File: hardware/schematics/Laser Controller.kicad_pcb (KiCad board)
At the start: 2 copper layers, 118 x 90 mm, 57 parts, among them J1 Micro_SD_Card, J2 PWR IN +5V, J3 PWR IN Galvo, U1 ESP32-S3-N16R8-DevKit, U10 DS18B20, U12 OPA4134UA_2K5, U13 Galvo Input, U15 6N137, U16 6N137, U17 6N137, U2 DAC8562SDGST, U3 TTL_RGB Blue, U4 TTL_RGB Red, U5 TTL_RGB Green, U6 DS18B20, U7 DS18B20, U8 DS18B20, U9 DS18B20

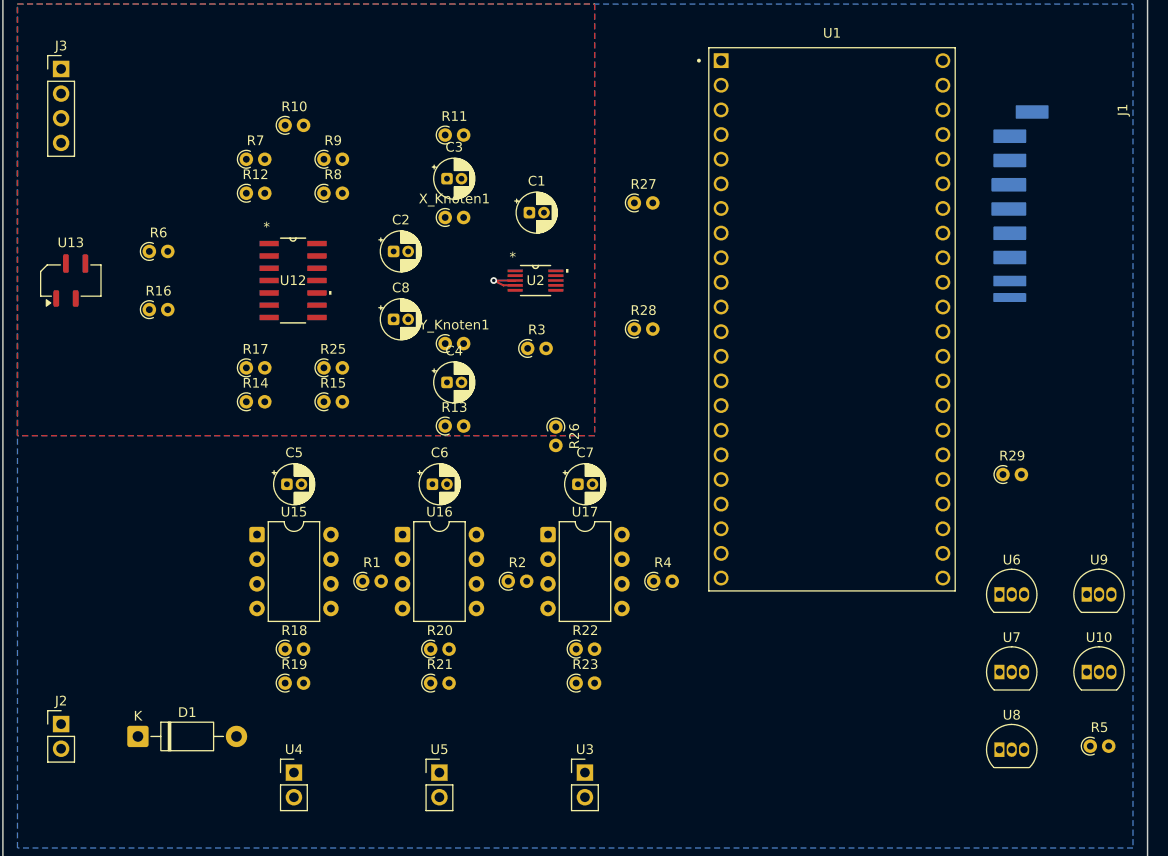
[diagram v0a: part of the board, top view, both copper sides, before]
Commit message: hw: copper happened - Freerouting did 92 nets in 19 seconds, 31 of them badly
Wired up the KiCAD MCP server and let Freerouting 2.0.1 loose on the board.
274 tracks, 10 vias, zero unconnected items. Not fab-ready: 31 clearance
violations survive, 20 of them under 0.10 mm, and they are not spread evenly -
they sit on the two fine-pitch parts where the router tried to thread traces
between pads that have no room between them.

- Added Laser Controller.kicad_pro with a Power net class and 0.2 mm design
  rules, so the board finally has somewhere to keep its rules
- Power traces widened after SES import: +-15V / 5V rails 0.6 mm, +3V3 and
  grounds 0.5 mm, signals stay at 0.2 mm
- Zones refilled after import - without that, DRC screams 283 zero-clearance
  errors that are pure artifact
- LAYOUT.md documents the remaining violations by location, plus two
  Freerouting quirks: it exports everything at a fixed 200 um in one
  kicad_default class (the Power net class never reaches it), and the SES
  import leaves pours unfilled
- .gitignore now swallows .dsn/.ses/.kicad_prl/DRC json

Next: rip up and hand-route the U2 and U12 fanouts. Worth doing by hand
regardless - an autorouter has no opinion about feedback loop length or which
side of a split ground plane a return current belongs on.
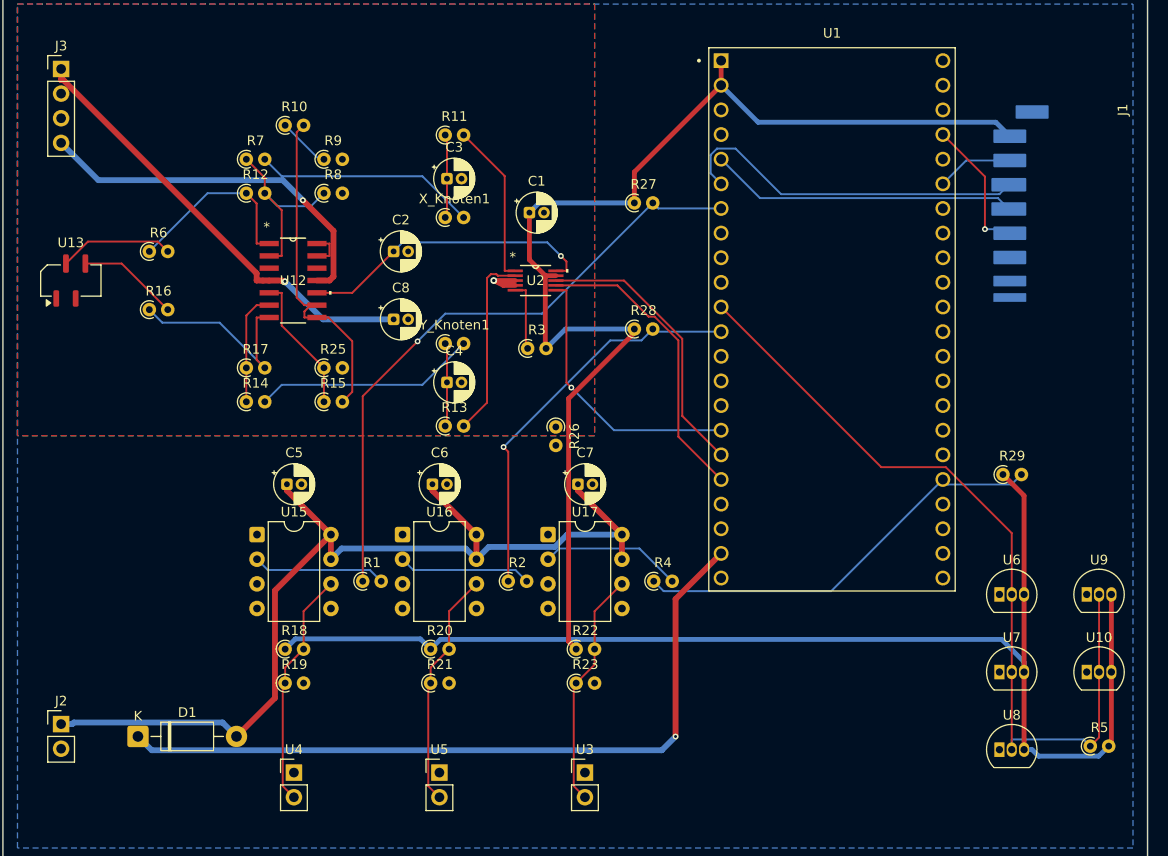
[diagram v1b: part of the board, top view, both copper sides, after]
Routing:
- net +3V3: track 0.00 -> 258.3 mm
- net Buck +5V: track 0.00 -> 104.4 mm
- net Net-(U1-GPIO18): track 0.00 -> 87.4 mm
- net /+5V_MCU: track 0.00 -> 77.4 mm, vias 0 -> 1
- net /GPIO7: track 0.00 -> 64.5 mm, vias 0 -> 1
- net +15V: track 0.00 -> 46.1 mm, vias 0 -> 1
- net /GPIO21: track 0.00 -> 43.7 mm
- net /GPIO8: track 0.00 -> 41.6 mm, vias 0 -> 1
- net -15V: track 0.00 -> 38.4 mm, vias 0 -> 1
- net Net-(J1-MOSI): track 0.00 -> 36.8 mm
- net /VREF_BUF: track 0.00 -> 34.6 mm
- net Net-(J1-CLK): track 0.00 -> 31.8 mm
- net Net-(U1-GPIO12): track 0.00 -> 31.1 mm
- net Net-(U12-+IN_C): track 0.00 -> 30.7 mm, vias 0 -> 1
- net Net-(U1-GPIO11): track 0.00 -> 29.1 mm
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
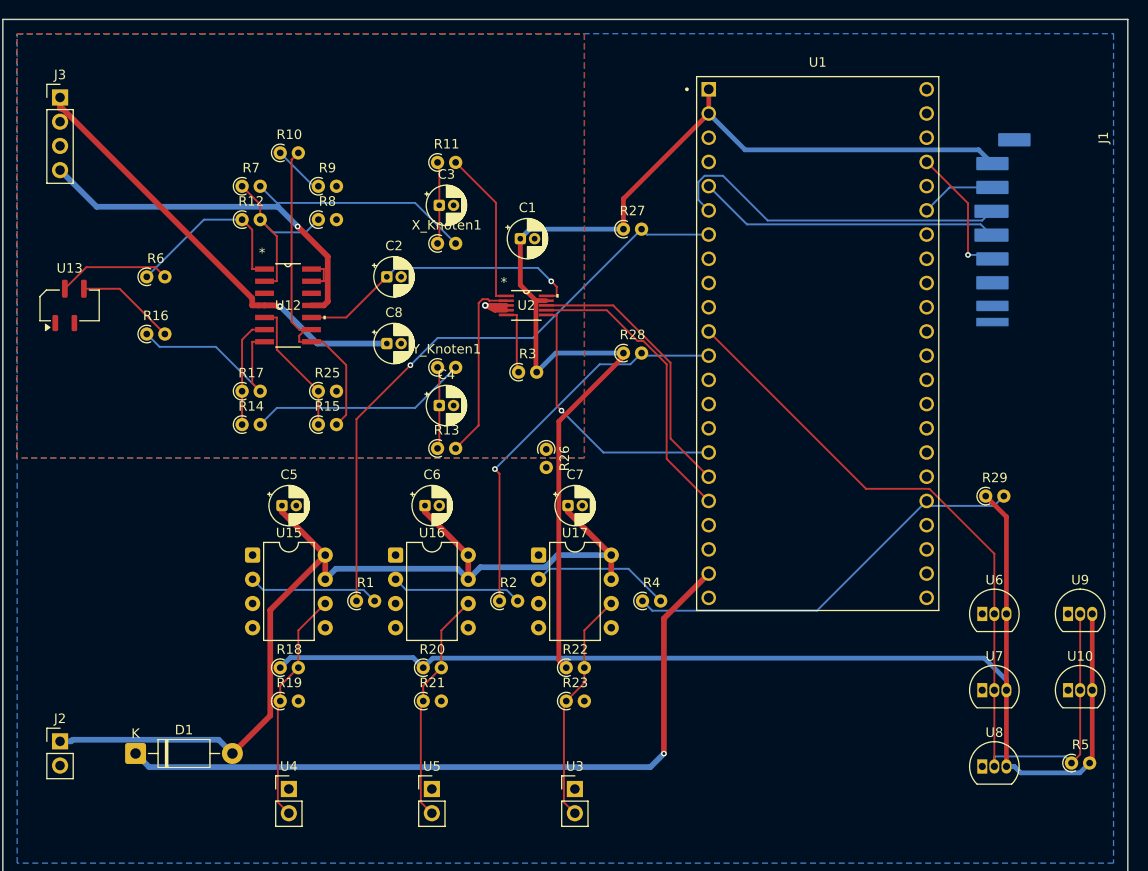
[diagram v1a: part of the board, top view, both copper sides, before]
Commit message: hw: DRC finally ran out of things to complain about - Gerbers shipped
Zero clearance violations, zero unconnected items, 257 tracks and 14 vias.
Gerbers and Excellon drills (187 plated holes, 0.3-1.1 mm) are in
hardware/gerbers/.

The 31 violations from the last commit had one cause and it was not the
fine-pitch parts being unroutable - the DSN export carries
"(clearance 50 (type smd_smd))", which tells Freerouting that 0.05 mm from an
SMD pad is perfectly fine. It took that offer, repeatedly, down to 0.0017 mm.
Removed the exception and raised the clearance.

Then the second cause, which was mine: widening the supply rails after import
moved every trace edge outward by 0.2 mm and ate the clearance the router had
just been taught to respect. The widening pass is now clearance-aware - each
track grows only as far as its nearest foreign pad, via or track permits, so
two traces beside U2 politely stay narrow.

- Routed at a deliberate 0.45 mm clearance, rails widened into that slack
  afterwards: signals 0.2 mm, supply rails 0.4 mm, grounds on the pours
- Freerouting ignores DSN net classes outright - a power class at width 500
  came back with every path still 200 um, so width cannot be set at route time
- Pours must be refilled after every SES import, else DRC invents 283
  zero-clearance errors from tracks lying on unfilled zone copper
- LAYOUT.md documents the whole export -> patch -> route -> import -> refill ->
  widen recipe so the next run does not rediscover all three traps

Left standing on purpose: 3 starved thermals (single spoke, still connected)
and 71 silkscreen overlaps. Neither blocks fabrication.
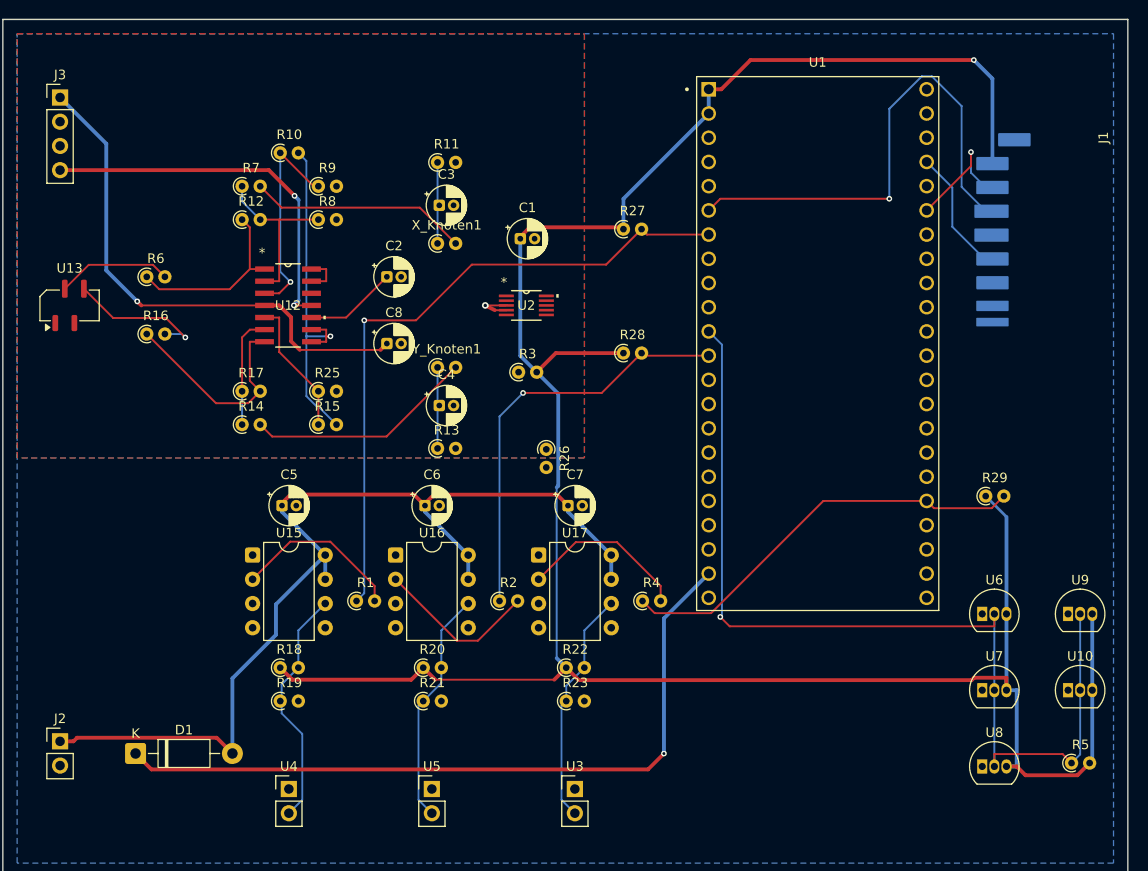
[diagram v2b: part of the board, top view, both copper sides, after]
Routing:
- net Net-(J1-CLK): track 31.8 -> 0.00 mm
- net Net-(U1-GPIO12): track 31.1 -> 0.00 mm
- net Net-(U1-GPIO11): track 29.1 -> 0.00 mm
- net Net-(U1-GPIO10): track 28.6 -> 0.00 mm, vias 1 -> 0
- net Net-(U12-+IN_C): track 30.7 -> 9.67 mm, vias 1 -> 0
- net Net-(U2-VOUTB): track 19.4 -> 0.00 mm
- net Net-(U12-+IN_A): track 5.45 -> 22.7 mm, vias 0 -> 1
- net Net-(U2-VOUTA): track 16.8 -> 0.00 mm
- net Net-(U1-GPIO18): track 87.4 -> 102.8 mm, vias 0 -> 1
- net Net-(J1-MOSI): track 36.8 -> 51.8 mm, vias 0 -> 1
- net +15V: track 46.1 -> 54.8 mm
- net Net-(U2-CLR): track 7.17 -> 0.00 mm
- net +3V3: track 258.3 -> 264.7 mm, vias 0 -> 1
- net /GPIO7: track 64.5 -> 70.1 mm
- net Net-(J1-CS): track 7.90 -> 13.1 mm, vias 0 -> 1
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
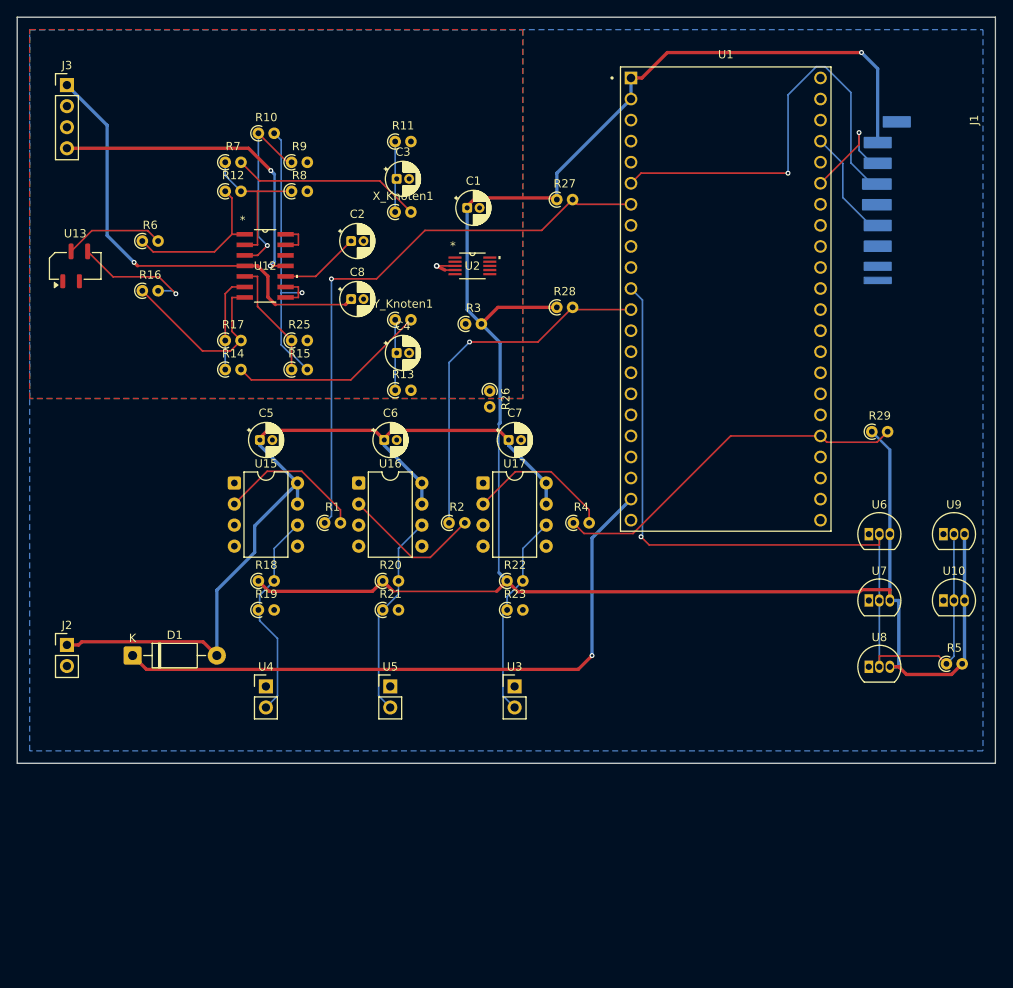
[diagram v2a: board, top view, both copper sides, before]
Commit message: hw: everything's JST XH now, the fans finally get a seat at the table
RGB, DS18B20 probes, +5V/+-15V supply and the galvo signal input all
standardized onto JST XH 2.54mm housings -- J3 and U13 lost a stray
unused pin in the process (4-pin -> clean 3-pin). Two fan sub-circuits
added from scratch (J4-J7, R30/R31): 2-pin JST power feed -> standard
4-pin PC-fan header, PWM straight off GPIO16/17 (no driver stage --
that's what a real 4-wire fan's PWM pin is for), TACH wired to the two
GPIOs that have been sitting free since the SD rewire (2 and 9),
hardware-only for now.

Board was full at 118x90, stretched to 118x115 for the new fan row.
Freerouting 2.2.4 did a full re-route (footprint swaps orphaned most
of the old copper), zones refilled, DRC down to 4 pre-existing
zone-corner nitpicks that have nothing to do with any of this.
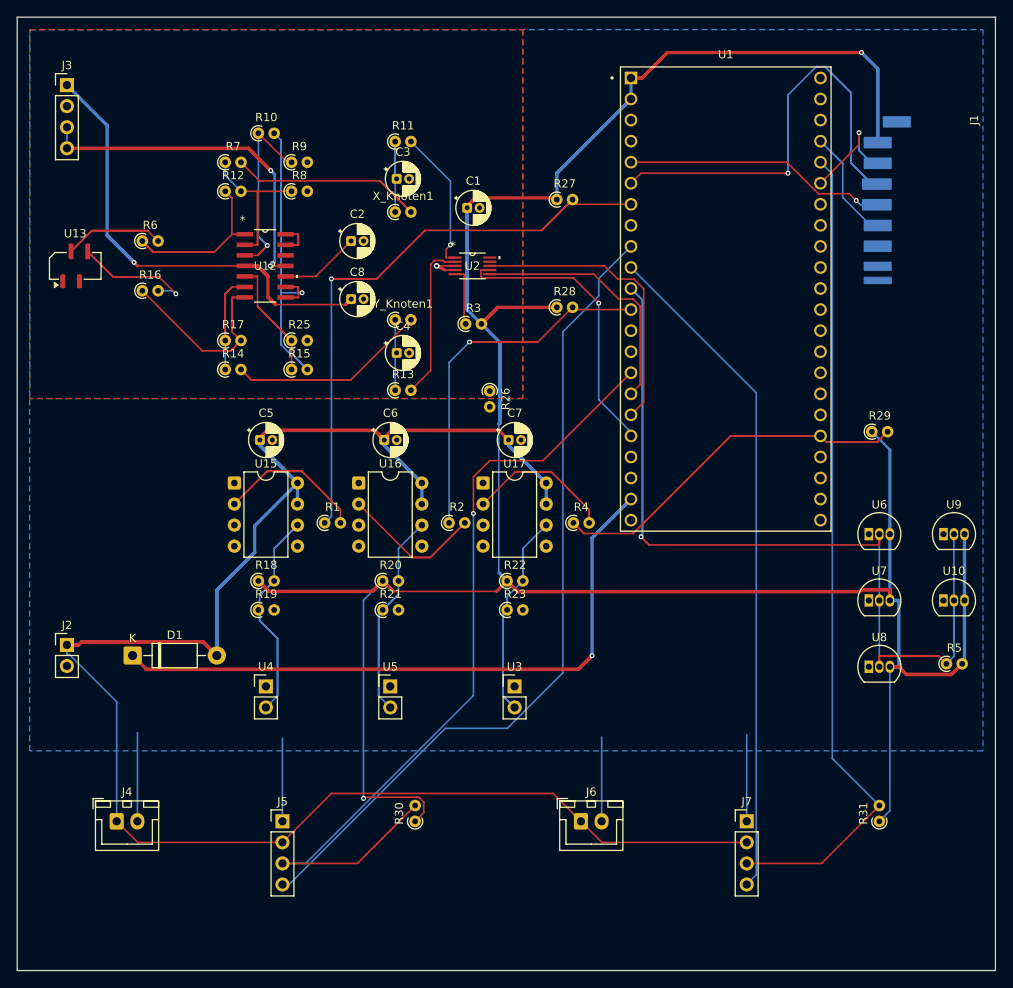
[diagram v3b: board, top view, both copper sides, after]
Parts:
- added J4: FAN1 PWR IN, Connector_JST:JST_XH_B2B-XH-A_1x02_P2.50mm_Vertical, F.Cu at (12.0, 97.0)
- added J5: FAN1, Connector_PinHeader_2.54mm:PinHeader_1x04_P2.54mm_Vertical, F.Cu at (32.0, 97.0)
- added J6: FAN2 PWR IN, Connector_JST:JST_XH_B2B-XH-A_1x02_P2.50mm_Vertical, F.Cu at (68.0, 97.0)
- added J7: FAN2, Connector_PinHeader_2.54mm:PinHeader_1x04_P2.54mm_Vertical, F.Cu at (88.0, 97.0)
- added R30: 4.7k, Resistor_THT:R_Axial_DIN0204_L3.6mm_D1.6mm_P1.90mm_Vertical, F.Cu at (48.0, 97.0)
- added R31: 4.7k, Resistor_THT:R_Axial_DIN0204_L3.6mm_D1.6mm_P1.90mm_Vertical, F.Cu at (104.0, 97.0)
- J2, U3, U4, U5: footprint PinHeader_1x02_P2.54mm_Vertical -> Connector_JST:JST_XH_B2B-XH-A_1x02_P2.50mm_Vertical
- J3: footprint PinHeader_1x04_P2.54mm_Vertical -> Connector_JST:JST_XH_B3B-XH-A_1x03_P2.50mm_Vertical
- U10, U6, U7, U8, U9: footprint TO-92_Inline -> Connector_JST:JST_XH_B3B-XH-A_1x03_P2.50mm_Vertical
- U13: footprint TE_84982-4_2Rows-04Pins-P1.0mm_Vertical -> Connector_JST:JST_XH_B3B-XH-A_1x03_P2.50mm_Vertical
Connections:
- net /+5V_MCU renamed +5V_MCU
- net /GPIO21 renamed GPIO21
- net /GPIO7 renamed GPIO7
- net /GPIO8 renamed GPIO8
- net /VREF_BUF renamed VREF_BUF
- J3 pad 3: AGND (from Galvo Board) -> -15V
- U1 pad J1_10: (no net) -> FAN2_PWM
- U1 pad J1_15: (no net) -> FAN1_TACH
- U1 pad J1_9: (no net) -> FAN1_PWM
- U1 pad J2_5: (no net) -> FAN2_TACH
- U13 pad 1: (no net) -> AGND (from Galvo Board)
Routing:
- net Buck +5V: track 104.7 -> 292.7 mm
- net +3V3: track 264.7 -> 398.9 mm, vias 1 -> 2
- net FAN1_TACH: track 0.00 -> 100.9 mm, vias 0 -> 1
- net FAN2_TACH: track 0.00 -> 99.4 mm
- net FAN1_PWM: track 0.00 -> 99.2 mm
- net FAN2_PWM: track 0.00 -> 81.2 mm
- net +5V_MCU: track 77.6 -> 138.7 mm
- net Net-(U1-GPIO18): track 102.8 -> 151.1 mm
- net 5V GND Buck: track 0.00 -> 41.3 mm
- net GPIO21: track 44.1 -> 81.3 mm
- net Net-(U1-GPIO11): track 0.00 -> 35.6 mm
- net Net-(U1-GPIO12): track 0.00 -> 35.0 mm, vias 0 -> 1
- net Net-(J1-CLK): track 0.00 -> 31.8 mm, vias 0 -> 1
- net Net-(U1-GPIO10): track 0.00 -> 30.8 mm
- net VREF_BUF: track 37.6 -> 67.1 mm
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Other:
- board size 118 x 90 mm -> 118 x 115 mm
